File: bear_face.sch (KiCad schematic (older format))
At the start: 197 parts, among them J1 USB_B_Micro, J2 Conn_02x03_Odd_Even, Q1 2N7002, SW1 SW_Push, U1 ATmega32U4-AU, U2 SRV05-4, Y1 16MHz

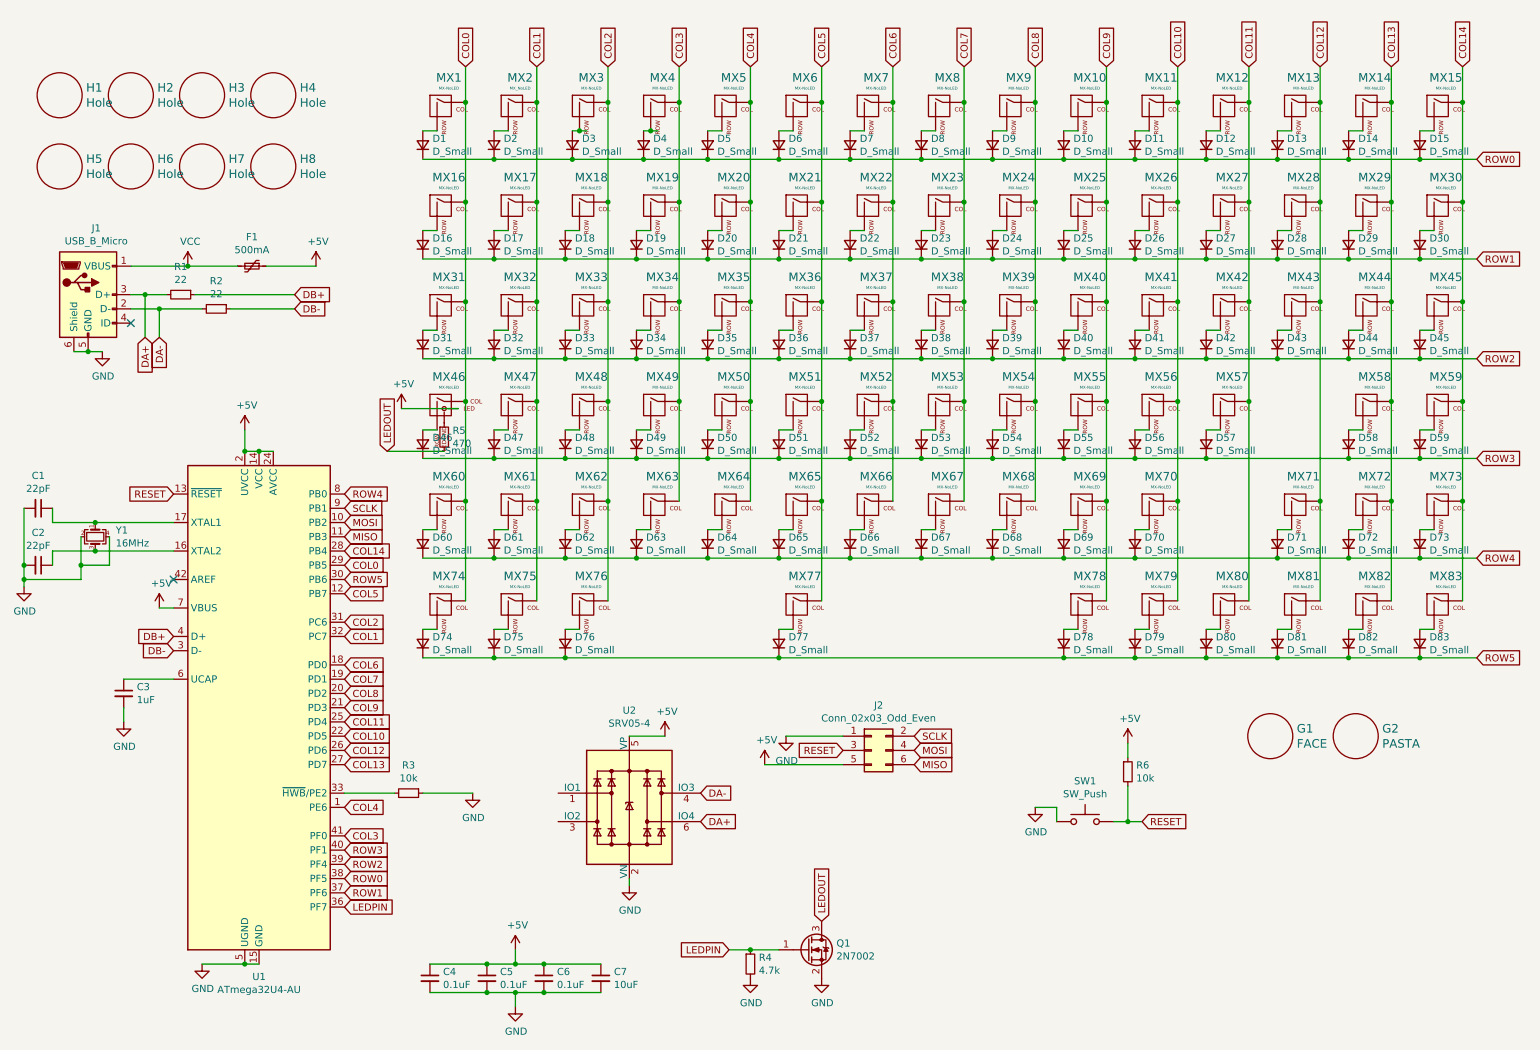
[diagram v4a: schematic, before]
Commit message: LCSC#s added to schematic
C codes added for SMT assembly pick and place
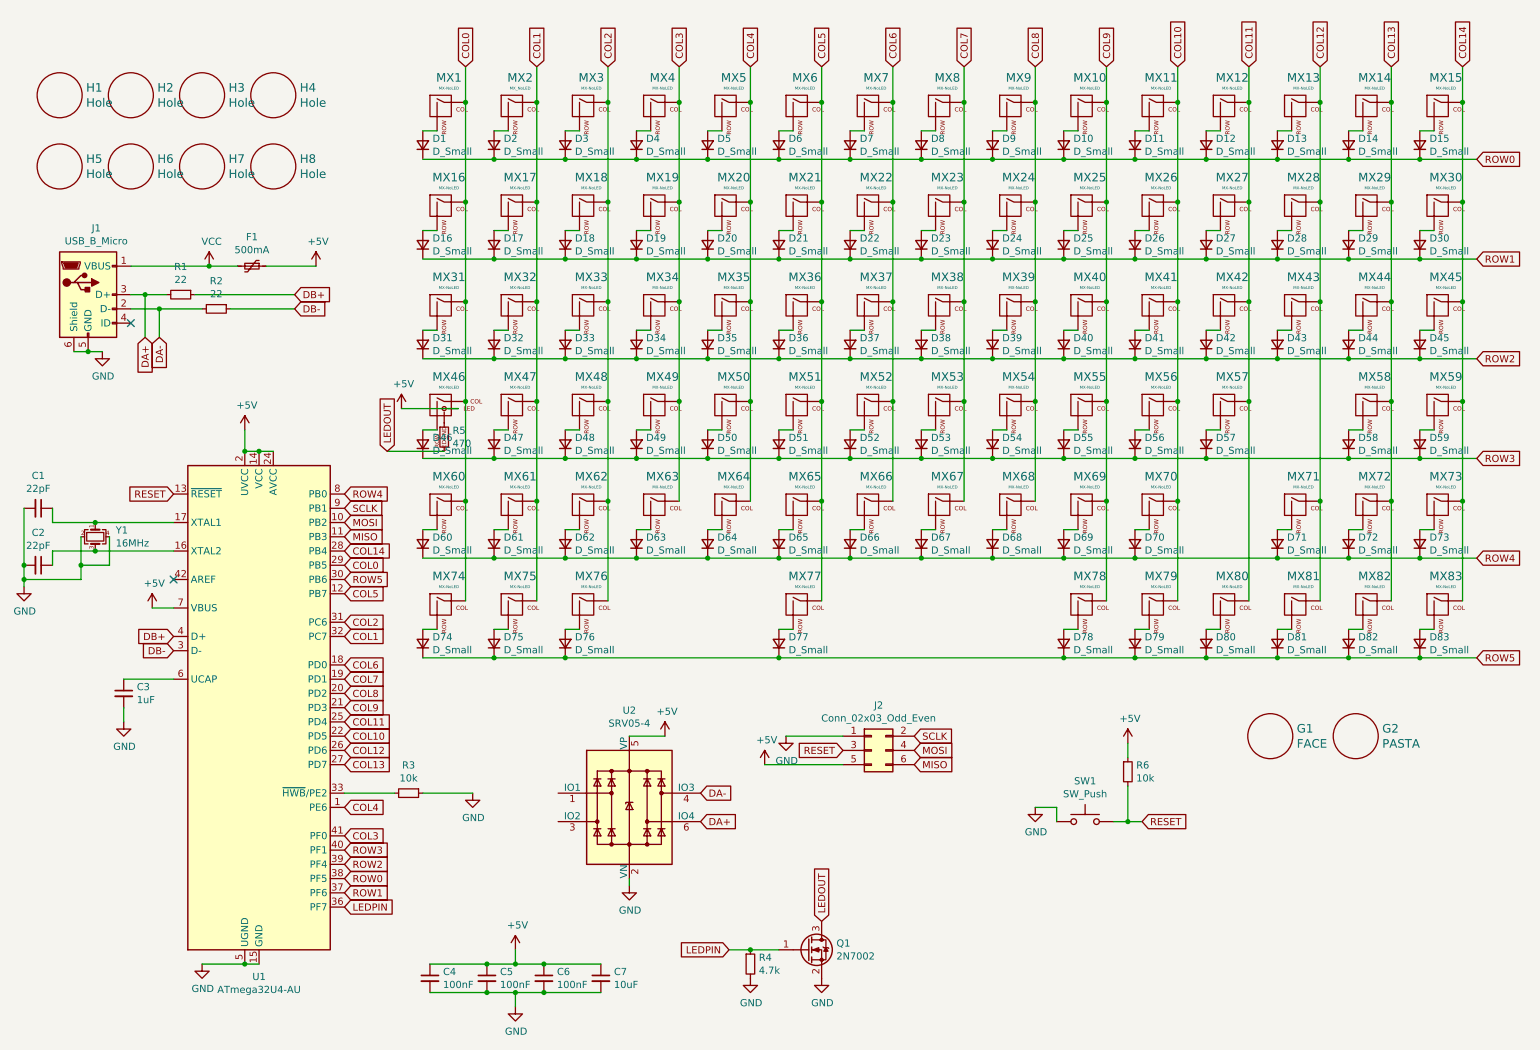
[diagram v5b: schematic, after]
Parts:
- C1, C2: LCSC# (none) -> C1804
- C3: LCSC# (none) -> C28323
- C4, C5, C6: value 0.1uF -> 100nF; LCSC# (none) -> C49678
- C7: LCSC# (none) -> C15850
- D1, D2: LCSC# C81598 -> C81598
- D10, D11, D12, D13, D14, D15, D16, D17, D18, D19, D20, D21, D22, D23, D24, D25, D26, D27, D28, D29, D3, D30, D31, D32, D33, D34, D35, D36, D37, D38, D39, D4, D40, D41, D42, D43, D44, D45, D46, D47, D48, D49, D5, D50, D51, D52, D53, D54, D55, D56, D57, D58, D59, D6, D60, D61, D62, D63, D64, D65, D66, D67, D68, D69, D7, D70, D71, D72, D73, D74, D75, D76, D77, D78, D79, D8, D80, D81, D82, D83, D9: LCSC# (none) -> C81598
- F1: LCSC# (none) -> C151162
- Q1: LCSC# (none) -> C8545
- R1, R2: LCSC# (none) -> C17561
- R3, R6: LCSC# (none) -> C17414
- R4: LCSC# (none) -> C17673
- R5: LCSC# (none) -> C17710
- U1: LCSC# (none) -> C44854
- U2: LCSC# (none) -> C85364
- Y1: LCSC# (none) -> C89379
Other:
- moved on the sheet: D3, D4

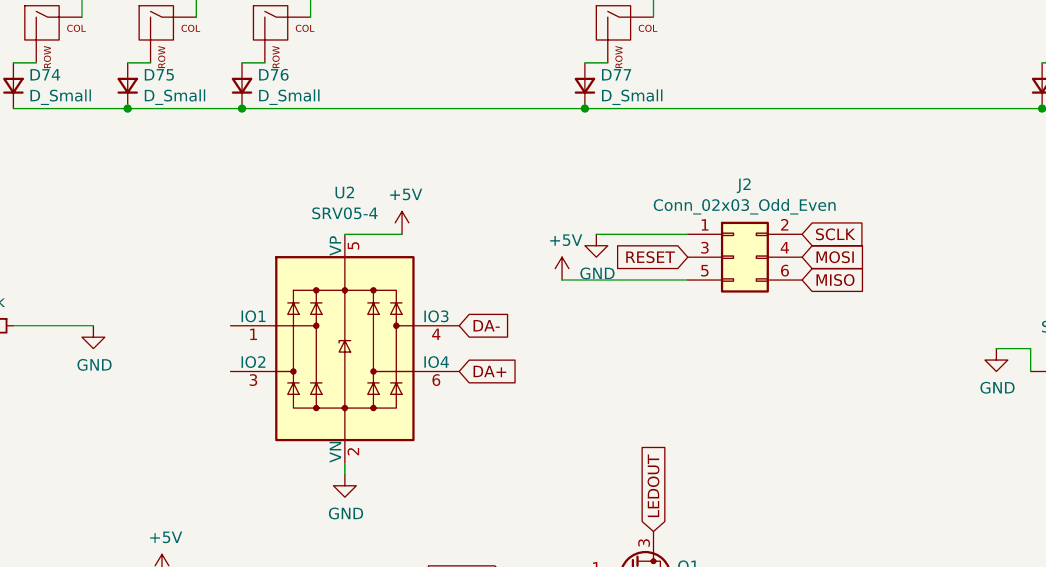
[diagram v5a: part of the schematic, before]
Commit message: Changed 2x3 pins, re-routed
Old gerbers deleted
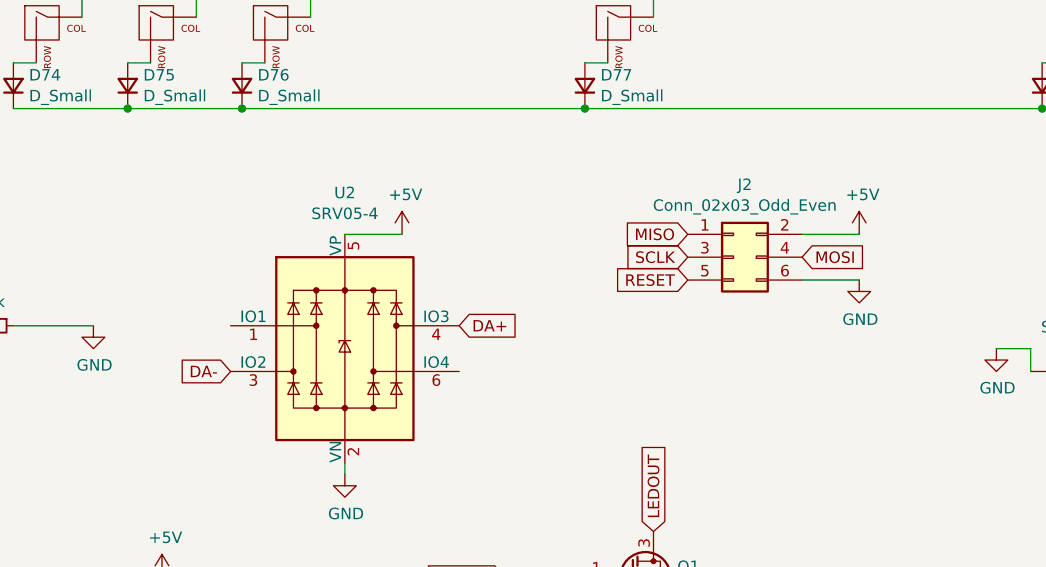
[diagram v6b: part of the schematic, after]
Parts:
- J2: footprint Connector_PinSocket_2.54mm:PinSocket_2x03_P2.54mm_Vertical -> bear_face_parts:2x3pinsocketOFFSET
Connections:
- net +5V: now also J2.2 (Pin_2); no longer J2.5 (Pin_5)
- net DA+: now also U2.4 (IO3); no longer U2.6 (IO4)
- net DA-: now also U2.3 (IO2); no longer U2.4 (IO3)
- net GND: now also J2.6 (Pin_6); no longer J2.1 (Pin_1)
- net MISO: now also J2.1 (Pin_1); no longer J2.6 (Pin_6)
- net RESET: now also J2.5 (Pin_5); no longer J2.3 (Pin_3)
- net SCLK: now also J2.3 (Pin_3); no longer J2.2 (Pin_2)
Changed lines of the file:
@@
 Wire Wire Line
 	5000 6550 5000 6500
+Text GLabel 4500 6100 0    50   Input ~ 0
+DA-
 Text GLabel 5500 5900 2    50   Input ~ 0
-DA-
-Text GLabel 5500 6100 2    50   Input ~ 0
 DA+
 Wire Wire Line
@@
 F 0 "J2" H 6750 5917 50  0000 C CNN
 F 1 "Conn_02x03_Odd_Even" H 6750 5826 50  0000 C CNN
-F 2 "Connector_PinSocket_2.54mm:PinSocket_2x03_P2.54mm_Vertical" H 6700 5600 50  0001 C CNN
+F 2 "bear_face_parts:2x3pinsocketOFFSET" H 6700 5600 50  0001 C CNN
 F 3 "~" H 6700 5600 50  0001 C CNN
 	1    6700 5600
 	1    0    0    -1
 $EndComp
-Text GLabel 7000 5500 2    50   Input ~ 0
+Text GLabel 6500 5600 0    50   Input ~ 0
 SCLK
 Text GLabel 7000 5600 2    50   Input ~ 0
 MOSI
-Text GLabel 7000 5700 2    50   Input ~ 0
+Text GLabel 6500 5500 0    50   Input ~ 0
 MISO
 Text GLabel 8600 6100 2    50   Input ~ 0
@@
 Text GLabel 1800 3800 0    50   Input ~ 0
 RESET
-Text GLabel 6500 5600 0    50   Input ~ 0
+Text GLabel 6500 5700 0    50   Input ~ 0
 RESET
-Wire Wire Line
-	6500 5500 6100 5500
 $Comp
 L power:GND #PWR0105
 U 1 1 5E4F520E
-P 6100 5500
-F 0 "#PWR0105" H 6100 5250 50  0001 C CNN
-F 1 "GND" H 6105 5327 50  0000 C CNN
-F 2 "" H 6100 5500 50  0001 C CNN
-F 3 "" H 6100 5500 50  0001 C CNN
-	1    6100 5500
-	1    0    0    -1
-$EndComp
-Wire Wire Line
-	6500 5700 5950 5700
+P 7250 5700
+F 0 "#PWR0105" H 7250 5450 50  0001 C CNN
+F 1 "GND" H 7255 5527 50  0000 C CNN
+F 2 "" H 7250 5700 50  0001 C CNN
+F 3 "" H 7250 5700 50  0001 C CNN
+	1    7250 5700
+	1    0    0    -1
+$EndComp
 $Comp
 L power:+5V #PWR0106
 U 1 1 5E54EE72
-P 5950 5700
-F 0 "#PWR0106" H 5950 5550 50  0001 C CNN
-F 1 "+5V" H 5965 5873 50  0000 C CNN
-F 2 "" H 5950 5700 50  0001 C CNN
-F 3 "" H 5950 5700 50  0001 C CNN
-	1    5950 5700
+P 7250 5500
+F 0 "#PWR0106" H 7250 5350 50  0001 C CNN
+F 1 "+5V" H 7265 5673 50  0000 C CNN
+F 2 "" H 7250 5500 50  0001 C CNN
+F 3 "" H 7250 5500 50  0001 C CNN
+	1    7250 5500
 	1    0    0    -1
 $EndComp
@@
 Wire Wire Line
 	1650 4600 1800 4600
+Wire Wire Line
+	7000 5500 7250 5500
+Wire Wire Line
+	7000 5700 7250 5700
 $EndSCHEMATC

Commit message: Added optional stepped Caps Lock support
* Same spot in the matrix, traced to allow either switch position
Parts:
- MX46: footprint bear_face_parts:MXOnly-1.75U-CapsLED-XD75-socket -> bear_face_parts:MXOnly-Stepped-Caps-XD75-socket
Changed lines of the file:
@@
 F 0 "MX46" H 3733 3423 60  0000 C CNN
 F 1 "MX-NoLED" H 3733 3349 20  0000 C CNN
-F 2 "bear_face_parts:MXOnly-1.75U-CapsLED-XD75-socket" H 3075 3175 60  0001 C CNN
+F 2 "bear_face_parts:MXOnly-Stepped-Caps-XD75-socket" H 3075 3175 60  0001 C CNN
 F 3 "" H 3075 3175 60  0001 C CNN
 	1    3700 3200

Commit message: Added ISO Enter support
* ISO enter shares a matrix position with ANSI \|
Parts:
- MX44: footprint bear_face_parts:MXOnly-1.5U-NoLED -> bear_face_parts:MXOnly-ISO-slashpipe
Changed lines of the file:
@@
 F 0 "MX44" H 10233 2723 60  0000 C CNN
 F 1 "MX-NoLED" H 10233 2649 20  0000 C CNN
-F 2 "bear_face_parts:MXOnly-1.5U-NoLED" H 9575 2475 60  0001 C CNN
+F 2 "bear_face_parts:MXOnly-ISO-slashpipe" H 9575 2475 60  0001 C CNN
 F 3 "" H 9575 2475 60  0001 C CNN
 	1    10200 2500
